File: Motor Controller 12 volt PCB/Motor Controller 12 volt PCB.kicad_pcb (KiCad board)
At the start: 2 copper layers, 48.8 x 33.4 mm, 7 parts, among them J2 776279-1, K1 PR22-12V-400-1A

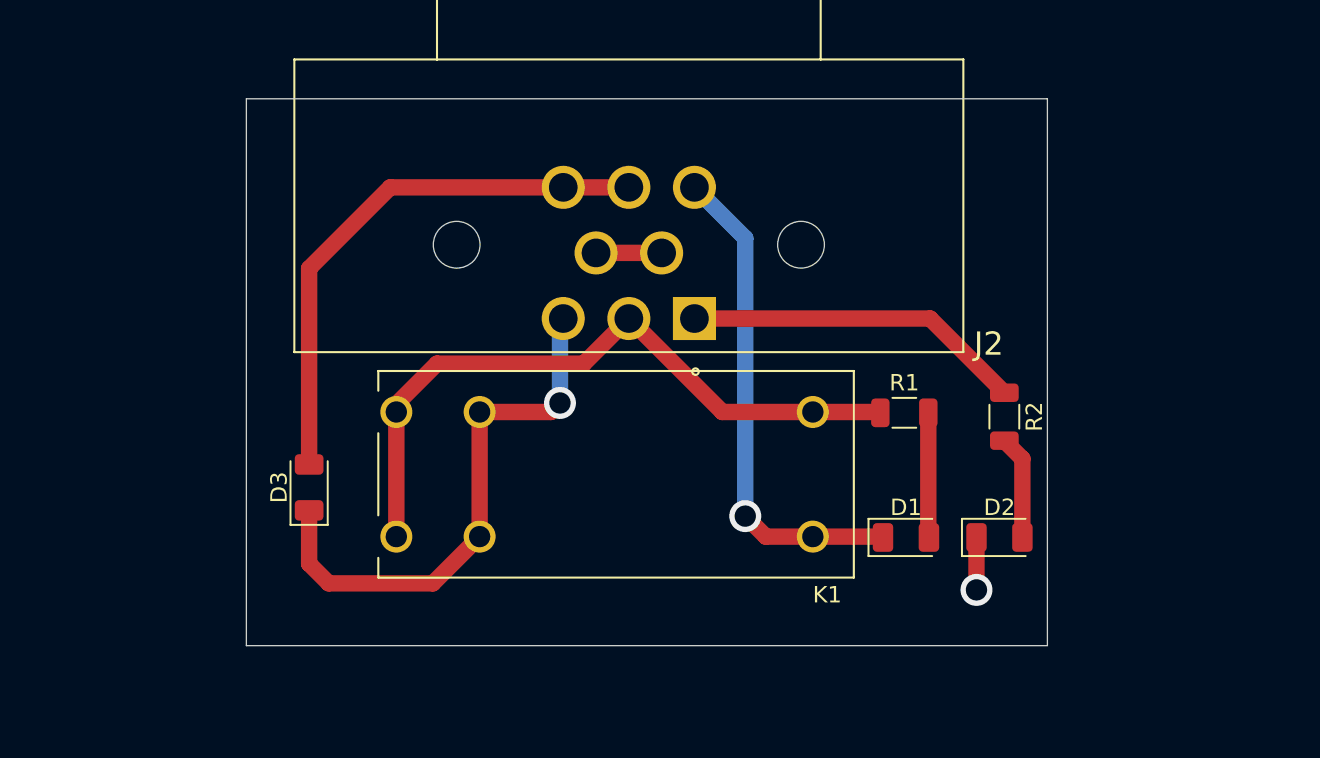
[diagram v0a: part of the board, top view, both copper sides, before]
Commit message: 12 v power supply pcb with mounting holes
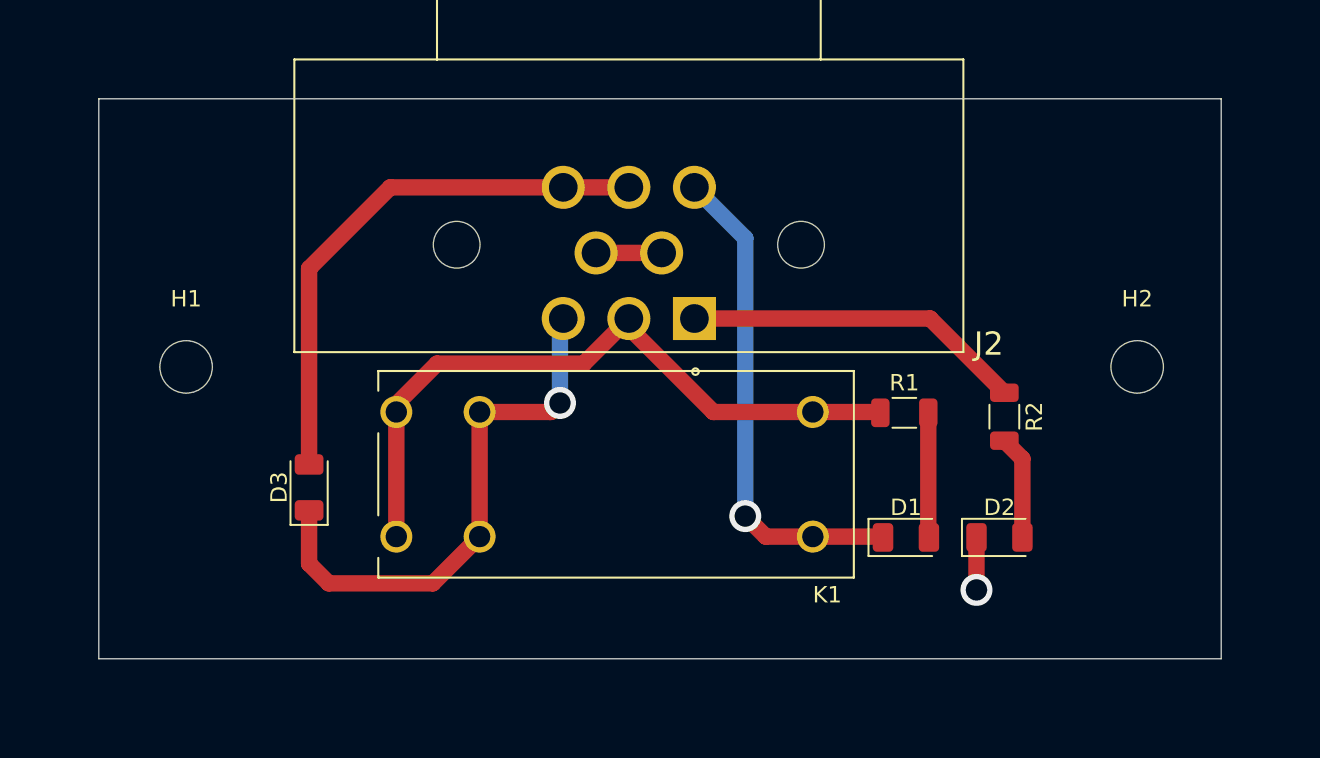
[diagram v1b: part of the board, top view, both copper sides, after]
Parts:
- added H1: MountingHole, MountingHole:MountingHole_3.2mm_M3, F.Cu at (122.2, 80.0)
- added H2: MountingHole, MountingHole:MountingHole_3.2mm_M3, F.Cu at (180.2, 80.0)
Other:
- board size 48.8 x 33.4 mm -> 68.4 x 34.1 mm
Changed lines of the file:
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@@
 		(property ki_fp_filters "LED* LED_SMD:* LED_THT:*")
 		(sheetname "/")
-		(sheetfile "Motor Controller Small starter pcb.kicad_sch")
+		(sheetfile "Motor Controller 12 volt PCB.kicad_sch")
 		(attr smd)
 		(fp_line
@@
 		)
 	)
+	(footprint "MountingHole:MountingHole_3.2mm_M3"
+		(layer "F.Cu")
+		(at 180.2 80)
+		(descr "Mounting Hole 3.2mm, M3, no annular, generated by kicad-footprint-generator mountinghole.py")
+		(tags "mountinghole M3")
+		(property "Reference" "H2"
+			(at 0 -4.15 0)
+			(layer "F.SilkS")
+			(effects
+				(font
+					(size 1 1)
+					(thickness 0.15)
+				)
+			)
+		)
+		(property "Value" "MountingHole"
+			(at 0 4.15 0)
+			(layer "F.Fab")
+			(hide yes)
+			(effects
+				(font
+					(size 1 1)
+					(thickness 0.15)
+				)
+			)
+		)
+		(property "Datasheet" "~"
+			(at 0 0 0)
+			(layer "F.Fab")
+			(hide yes)
+			(effects
+				(font
+					(size 1.27 1.27)
+					(thickness 0.15)
+				)
+			)
+		)
+		(property "Description" "Mounting Hole without connection"
+			(at 0 0 0)
+			(layer "F.Fab")
+			(hide yes)
+			(effects
+				(font
+					(size 1.27 1.27)
+					(thickness 0.15)
+				)
+			)
+		)
+		(property ki_fp_filters "MountingHole*")
+		(sheetname "/")
+		(sheetfile "Motor Controller 12 volt PCB.kicad_sch")
+		(attr exclude_from_pos_files exclude_from_bom)
+		(fp_circle
+			(center 0 0)
+			(end 3.2 0)
+			(stroke
+				(width 0.15)
+				(type solid)
+			)
+			(fill no)
+			(layer "Cmts.User")
+		)
+		(fp_circle
+			(center 0 0)
+			(end 3.45 0)
+			(stroke
+				(width 0.05)
+				(type solid)
+			)
+			(fill no)
+			(layer "F.CrtYd")
+		)
+		(fp_text user "${REFERENCE}"
+			(at 0 0 0)
+			(layer "F.Fab")
+			(effects
+				(font
+					(size 1 1)
+					(thickness 0.15)
+				)
+			)
+		)
+		(pad "" np_thru_hole circle
+			(at 0 0)
+			(size 3.2 3.2)
+			(drill 3.2)
+			(layers "*.Cu" "*.Mask")
+		)
+		(embedded_fonts no)
+	)
 	(footprint "LED_SMD:LED_1206_3216Metric"
 		(layer "F.Cu")
@@
 		(property ki_fp_filters "LED* LED_SMD:* LED_THT:*")
 		(sheetname "/")
-		(sheetfile "Motor Controller Small starter pcb.kicad_sch")
+		(sheetfile "Motor Controller 12 volt PCB.kicad_sch")
 		(attr smd)
 		(fp_line
@@
 		(property ki_fp_filters "R_*")
 		(sheetname "/")
-		(sheetfile "Motor Controller Small starter pcb.kicad_sch")
+		(sheetfile "Motor Controller 12 volt PCB.kicad_sch")
 		(attr smd)
 		(fp_line
@@
 		(property ki_fp_filters "CR_SOD-523F_ONS CR_SOD-523F_ONS-M CR_SOD-523F_ONS-L")
 		(sheetname "/")
-		(sheetfile "Motor Controller Small starter pcb.kicad_sch")
+		(sheetfile "Motor Controller 12 volt PCB.kicad_sch")
 		(attr smd)
 		(fp_line
@@
 		)
 		(sheetname "/")
-		(sheetfile "Motor Controller Small starter pcb.kicad_sch")
+		(sheetfile "Motor Controller 12 volt PCB.kicad_sch")
 		(attr through_hole)
 		(fp_line
@@
 		)
 		(sheetname "/")
-		(sheetfile "Motor Controller Small starter pcb.kicad_sch")
+		(sheetfile "Motor Controller 12 volt PCB.kicad_sch")
 		(attr through_hole)
 		(fp_line
@@
 		)
 	)
+	(footprint "MountingHole:MountingHole_3.2mm_M3"
+		(layer "F.Cu")
+		(at 122.2 80)
+		(descr "Mounting Hole 3.2mm, M3, no annular, generated by kicad-footprint-generator mountinghole.py")
+		(tags "mountinghole M3")
+		(property "Reference" "H1"
+			(at 0 -4.15 0)
+			(layer "F.SilkS")
+			(effects
+				(font
+					(size 1 1)
+					(thickness 0.15)
+				)
+			)
+		)
+		(property "Value" "MountingHole"
+			(at 0 4.15 0)
+			(layer "F.Fab")
+			(hide yes)
+			(effects
+				(font
+					(size 1 1)
+					(thickness 0.15)
+				)
+			)
+		)
+		(property "Datasheet" "~"
+			(at 0 0 0)
+			(layer "F.Fab")
+			(hide yes)
+			(effects
+				(font
+					(size 1.27 1.27)
+					(thickness 0.15)
+				)
+			)
+		)
+		(property "Description" "Mounting Hole without connection"
+			(at 0 0 0)
+			(layer "F.Fab")
+			(hide yes)
+			(effects
+				(font
+					(size 1.27 1.27)
+					(thickness 0.15)
+				)
+			)
+		)
+		(property ki_fp_filters "MountingHole*")
+		(sheetname "/")
+		(sheetfile "Motor Controller 12 volt PCB.kicad_sch")
+		(attr exclude_from_pos_files exclude_from_bom)
+		(fp_circle
+			(center 0 0)
+			(end 3.2 0)
+			(stroke
+				(width 0.15)
+				(type solid)
+			)
+			(fill no)
+			(layer "Cmts.User")
+		)
+		(fp_circle
+			(center 0 0)
+			(end 3.45 0)
+			(stroke
+				(width 0.05)
+				(type solid)
+			)
+			(fill no)
+			(layer "F.CrtYd")
+		)
+		(fp_text user "${REFERENCE}"
+			(at 0 0 0)
+			(layer "F.Fab")
+			(effects
+				(font
+					(size 1 1)
+					(thickness 0.15)
+				)
+			)
+		)
+		(pad "" np_thru_hole circle
+			(at 0 0)
+			(size 3.2 3.2)
+			(drill 3.2)
+			(layers "*.Cu" "*.Mask")
+		)
+		(embedded_fonts no)
+	)
 	(footprint "Resistor_SMD:R_1206_3216Metric"
 		(layer "F.Cu")
@@
 		(property ki_fp_filters "R_*")
 		(sheetname "/")
-		(sheetfile "Motor Controller Small starter pcb.kicad_sch")
+		(sheetfile "Motor Controller 12 volt PCB.kicad_sch")
 		(attr smd)
 		(fp_line
@@
 	)
 	(gr_rect
-		(start 125.875 63.65)
-		(end 174.725 97)
+		(start 116.875 63.65)
+		(end 185.325 97.8)
 		(stroke
 			(width 0.05)
@@
 	)
 	(segment
+		(start 154.35 82.75)
+		(end 149.2 77.6)
+		(width 1)
+		(layer "F.Cu")
+		(net 9)
+	)
+	(segment
 		(start 164.4875 82.75)
 		(end 164.5375 82.8)
@@
 	)
 	(segment
-		(start 154.9 82.75)
-		(end 149.2 77.05)
-		(width 1)
-		(layer "F.Cu")
-		(net 9)
-	)
-	(segment
 		(start 137.5 79.8)
 		(end 146.45 79.8)
@@
 	)
 	(segment
+		(start 160.42 82.75)
+		(end 154.35 82.75)
+		(width 1)
+		(layer "F.Cu")
+		(net 9)
+	)
+	(segment
 		(start 135.02 82.28)
 		(end 137.5 79.8)
@@
 	)
 	(segment
+		(start 149.2 77.6)
+		(end 149.2 77.05)
+		(width 1)
+		(layer "F.Cu")
+		(net 9)
+	)
+	(segment
 		(start 146.45 79.8)
 		(end 149.2 77.05)
 		(width 1)
 		(layer "F.Cu")
-		(net 9)
-	)
-	(segment
-		(start 160.42 82.75)
-		(end 154.9 82.75)
-		(width 1)
-		(layer "F.Cu")

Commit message: Fully Updated 12 V PCB with correct Gerber Files
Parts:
- moved H2 12.1 mm to (176.4, 68.5)
- moved H1 11.7 mm to (124.4, 68.5)
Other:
- board size 68.4 x 34.1 mm -> 61.3 x 31.2 mm
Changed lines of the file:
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@@
 			(outputformat 1)
 			(mirror no)
-			(drillshape 1)
+			(drillshape 0)
 			(scaleselection 1)
-			(outputdirectory "")
+			(outputdirectory "Gerber/")
 		)
 	)
@@
 	(footprint "MountingHole:MountingHole_3.2mm_M3"
 		(layer "F.Cu")
-		(at 180.2 80)
+		(at 176.4 68.5)
 		(descr "Mounting Hole 3.2mm, M3, no annular, generated by kicad-footprint-generator mountinghole.py")
 		(tags "mountinghole M3")
 		(property "Reference" "H2"
-			(at 0 -4.15 0)
-			(layer "F.SilkS")
+			(at -0.1 -9.2 0)
+			(layer "F.SilkS")
+			(hide yes)
 			(effects
 				(font
@@
 	(footprint "MountingHole:MountingHole_3.2mm_M3"
 		(layer "F.Cu")
-		(at 122.2 80)
+		(at 124.4 68.5)
 		(descr "Mounting Hole 3.2mm, M3, no annular, generated by kicad-footprint-generator mountinghole.py")
 		(tags "mountinghole M3")
 		(property "Reference" "H1"
-			(at 0 -4.15 0)
-			(layer "F.SilkS")
+			(at 0.2 -6.5 0)
+			(layer "F.SilkS")
+			(hide yes)
 			(effects
 				(font
@@
 		)
 	)
-	(gr_rect
-		(start 116.875 63.65)
-		(end 185.325 97.8)
+	(gr_line
+		(start 124.091091 72.9)
+		(end 121.7 72.9)
 		(stroke
 			(width 0.05)
 			(type default)
 		)
-		(fill no)
 		(layer "Edge.Cuts")
 	)
+	(gr_arc
+		(start 121.7 72.9)
+		(mid 120.285786 72.314214)
+		(end 119.7 70.9)
+		(stroke
+			(width 0.05)
+			(type default)
+		)
+		(layer "Edge.Cuts")
+	)
+	(gr_line
+		(start 121.7 64.2)
+		(end 179 64.2)
+		(stroke
+			(width 0.05)
+			(type default)
+		)
+		(layer "Edge.Cuts")
+	)
+	(gr_arc
+		(start 175.2 93.4)
+		(mid 174.614214 94.814214)
+		(end 173.2 95.4)
+		(stroke
+			(width 0.05)
+			(type default)
+		)
+		(layer "Edge.Cuts")
+	)
+	(gr_line
+		(start 119.7 70.9)
+		(end 119.7 66.2)
+		(stroke
+			(width 0.05)
+			(type default)
+		)
+		(layer "Edge.Cuts")
+	)
+	(gr_arc
+		(start 179 64.2)
+		(mid 180.414214 64.785786)
+		(end 181 66.2)
+		(stroke
+			(width 0.05)
+			(type default)
+		)
+		(layer "Edge.Cuts")
+	)
+	(gr_arc
+		(start 124.091091 72.9)
+		(mid 125.50845 73.488929)
+		(end 126.091072 74.908889)
+		(stroke
+			(width 0.05)
+			(type default)
+		)
+		(layer "Edge.Cuts")
+	)
+	(gr_line
+		(start 175.2 74.9)
+		(end 175.2 93.4)
+		(stroke
+			(width 0.05)
+			(type default)
+		)
+		(layer "Edge.Cuts")
+	)
+	(gr_line
+		(start 179 72.9)
+		(end 177.2 72.9)
+		(stroke
+			(width 0.05)
+			(type default)
+		)
+		(layer "Edge.Cuts")
+	)
+	(gr_arc
+		(start 119.7 66.2)
+		(mid 120.285786 64.785786)
+		(end 121.7 64.2)
+		(stroke
+			(width 0.05)
+			(type default)
+		)
+		(layer "Edge.Cuts")
+	)
+	(gr_arc
+		(start 175.2 74.9)
+		(mid 175.785786 73.485786)
+		(end 177.2 72.9)
+		(stroke
+			(width 0.05)
+			(type default)
+		)
+		(layer "Edge.Cuts")
+	)
+	(gr_arc
+		(start 181 70.9)
+		(mid 180.414214 72.314214)
+		(end 179 72.9)
+		(stroke
+			(width 0.05)
+			(type default)
+		)
+		(layer "Edge.Cuts")
+	)
+	(gr_line
+		(start 173.2 95.4)
+		(end 128.008909 95.4)
+		(stroke
+			(width 0.05)
+			(type default)
+		)
+		(layer "Edge.Cuts")
+	)
+	(gr_line
+		(start 126.008928 93.391111)
+		(end 126.091072 74.908889)
+		(stroke
+			(width 0.05)
+			(type default)
+		)
+		(layer "Edge.Cuts")
+	)
+	(gr_arc
+		(start 128.008909 95.4)
+		(mid 126.591556 94.811067)
+		(end 126.008928 93.391111)
+		(stroke
+			(width 0.05)
+			(type default)
+		)
+		(layer "Edge.Cuts")
+	)
+	(gr_line
+		(start 181 66.2)
+		(end 181 70.9)
+		(stroke
+			(width 0.05)
+			(type default)
+		)
+		(layer "Edge.Cuts")
+	)
